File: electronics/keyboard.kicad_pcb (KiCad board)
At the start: 2 copper layers, 243 parts, among them CON1 AVR-ISP-6, J2 CONN_01X02_FEMALE, Q1 Q_NMOS_DGS, Q2 Q_NMOS_DGS, Q3 Q_PMOS_DGS, Q4 Q_NMOS_DGS, Q5 Q_PMOS_DGS, SW1 SW_DPST, SW10 SW_Push, SW11 SW_Push, SW12 SW_Push, SW13 SW_Push, SW14 SW_Push, SW15 SW_Push, SW16 SW_Push, SW17 SW_Push, SW18 SW_Push, SW19 SW_Push, SW2 SW_Push, SW20 SW_Push, SW21 SW_Push, SW22 SW_Push, SW23 SW_Push, SW24 SW_Push, SW25 SW_Push, SW26 SW_Push, SW27 SW_Push, SW28 SW_Push, SW29 SW_Push, SW3 SW_Push, SW30 SW_Push, SW31 SW_Push, SW32 SW_Push, SW33 SW_Push, SW34 SW_Push, SW35 SW_Push, SW36 SW_Push, SW37 SW_Push, SW38 SW_Push, SW39 SW_Push, SW4 SW_Push, SW40 SW_Push, SW41 SW_Push, SW42 SW_Push, SW43 SW_Push, SW44 SW_Push, SW45 SW_Push, SW46 SW_Push, SW47 SW_Push, SW48 SW_Push, SW49 SW_Push, SW5 SW_Push, SW50 SW_Push, SW51 SW_Push, SW52 SW_Push, SW53 SW_Push, SW54 SW_Push, SW55 SW_Push, SW56 SW_Push, SW57 SW_Push, SW58 SW_Push, SW59 SW_Push, SW6 SW_Push, SW60 SW_Push, SW61 SW_Push, SW62 SW_Push, SW63 SW_Push, SW64 SW_Push, SW65 SW_Push, SW66 SW_Push, SW67 SW_Push, SW68 SW_Push, SW69 SW_Push, SW7 SW_Push, SW70 SW_Push, SW71 SW_Push, SW72 SW_Push, SW73 SW_Push, SW74 SW_Push, SW75 SW_Push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

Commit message: Seperated the Buttons from the rest
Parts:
- moved SW43 658.1 mm to (-284.5, 58.4)
- moved SW44 623.4 mm to (-297.2, -77.5)
- moved SW47 623.4 mm to (-268.0, -99.1)
- moved SW42 600.7 mm to (-236.2, -3.81)
- moved SW26 583.9 mm to (-341.6, -88.9)
- moved SW48 578.1 mm to (-238.8, 27.9)
- moved SW12 541.4 mm to (-294.6, 29.2)
- moved SW89 492.8 mm to (-325.1, -41.9)
- moved SW90 492.8 mm to (-276.9, -50.8)
- moved SW91 492.8 mm to (-241.3, -43.2)
- moved SW88 492.8 mm to (-398.8, -41.9)
- moved SW55 421.7 mm to (-407.7, 63.5)
- moved SW56 421.7 mm to (-407.7, 81.3)
- moved SW30 421.7 mm to (-386.1, 8.89)
- moved SW54 421.7 mm to (-408.9, 40.6)
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
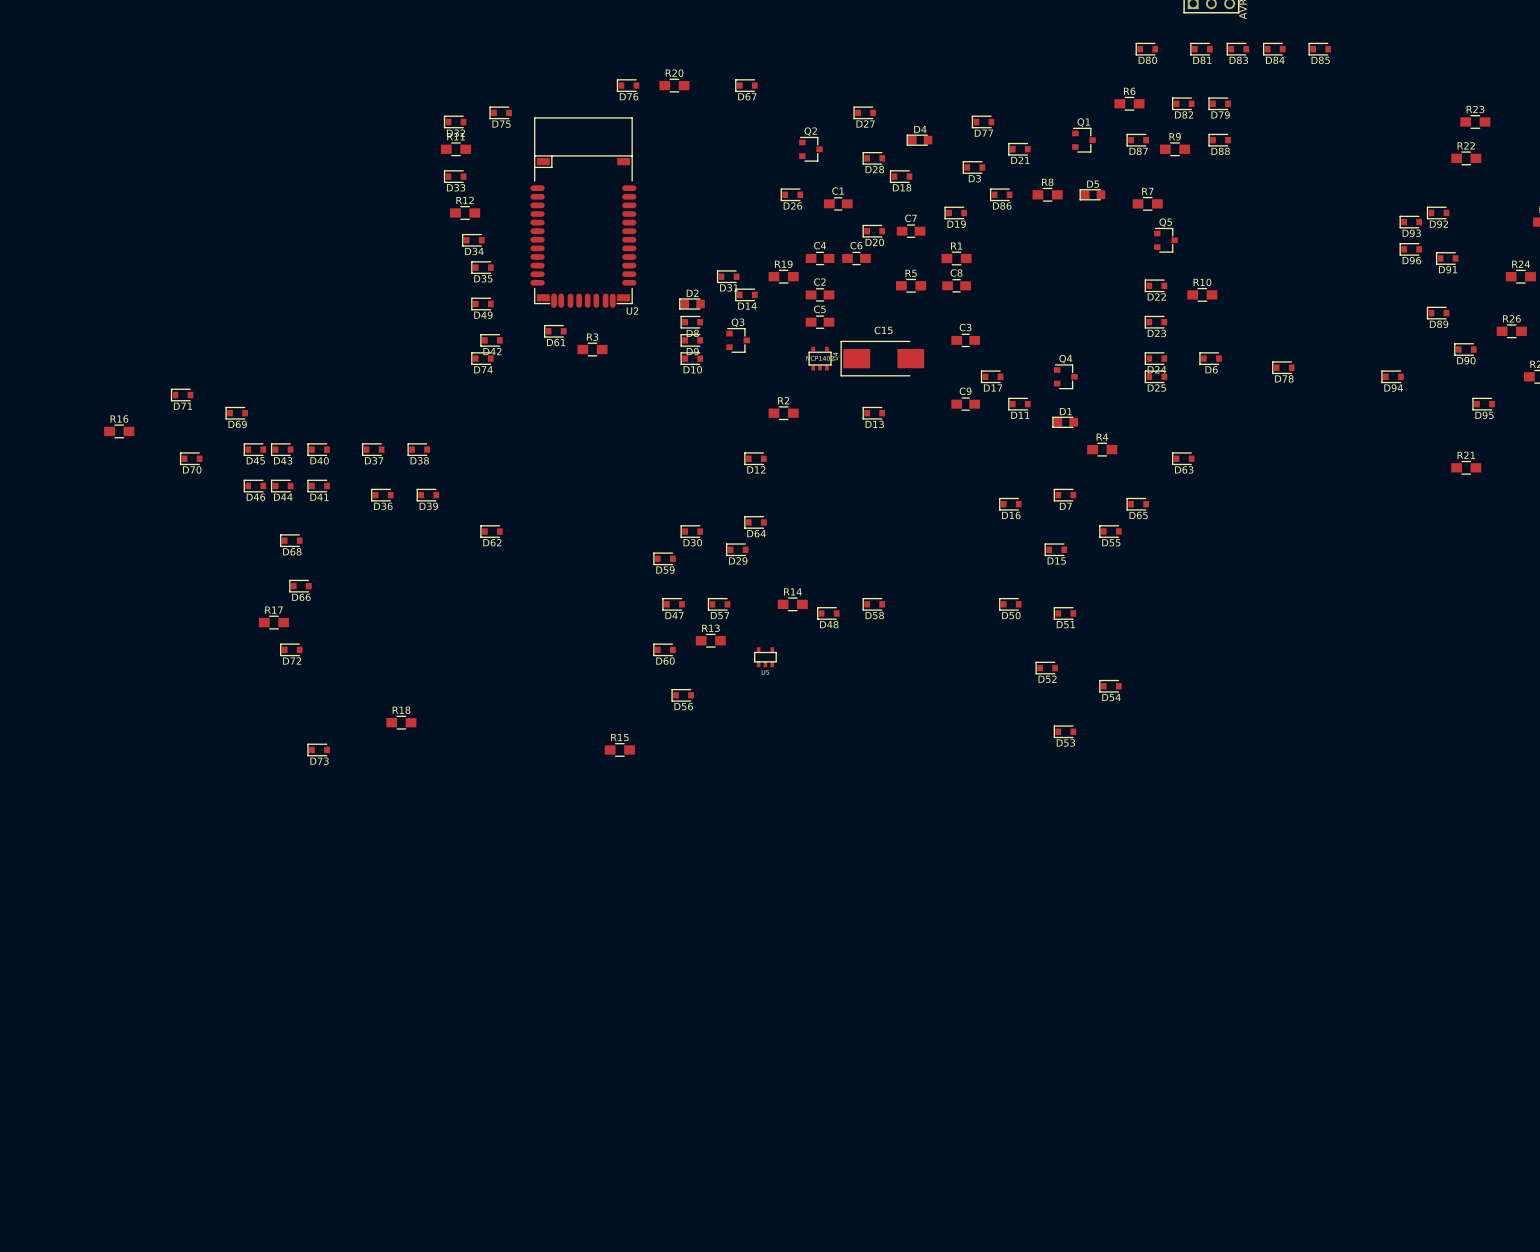
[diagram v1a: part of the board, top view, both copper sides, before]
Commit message: Seperated diodes
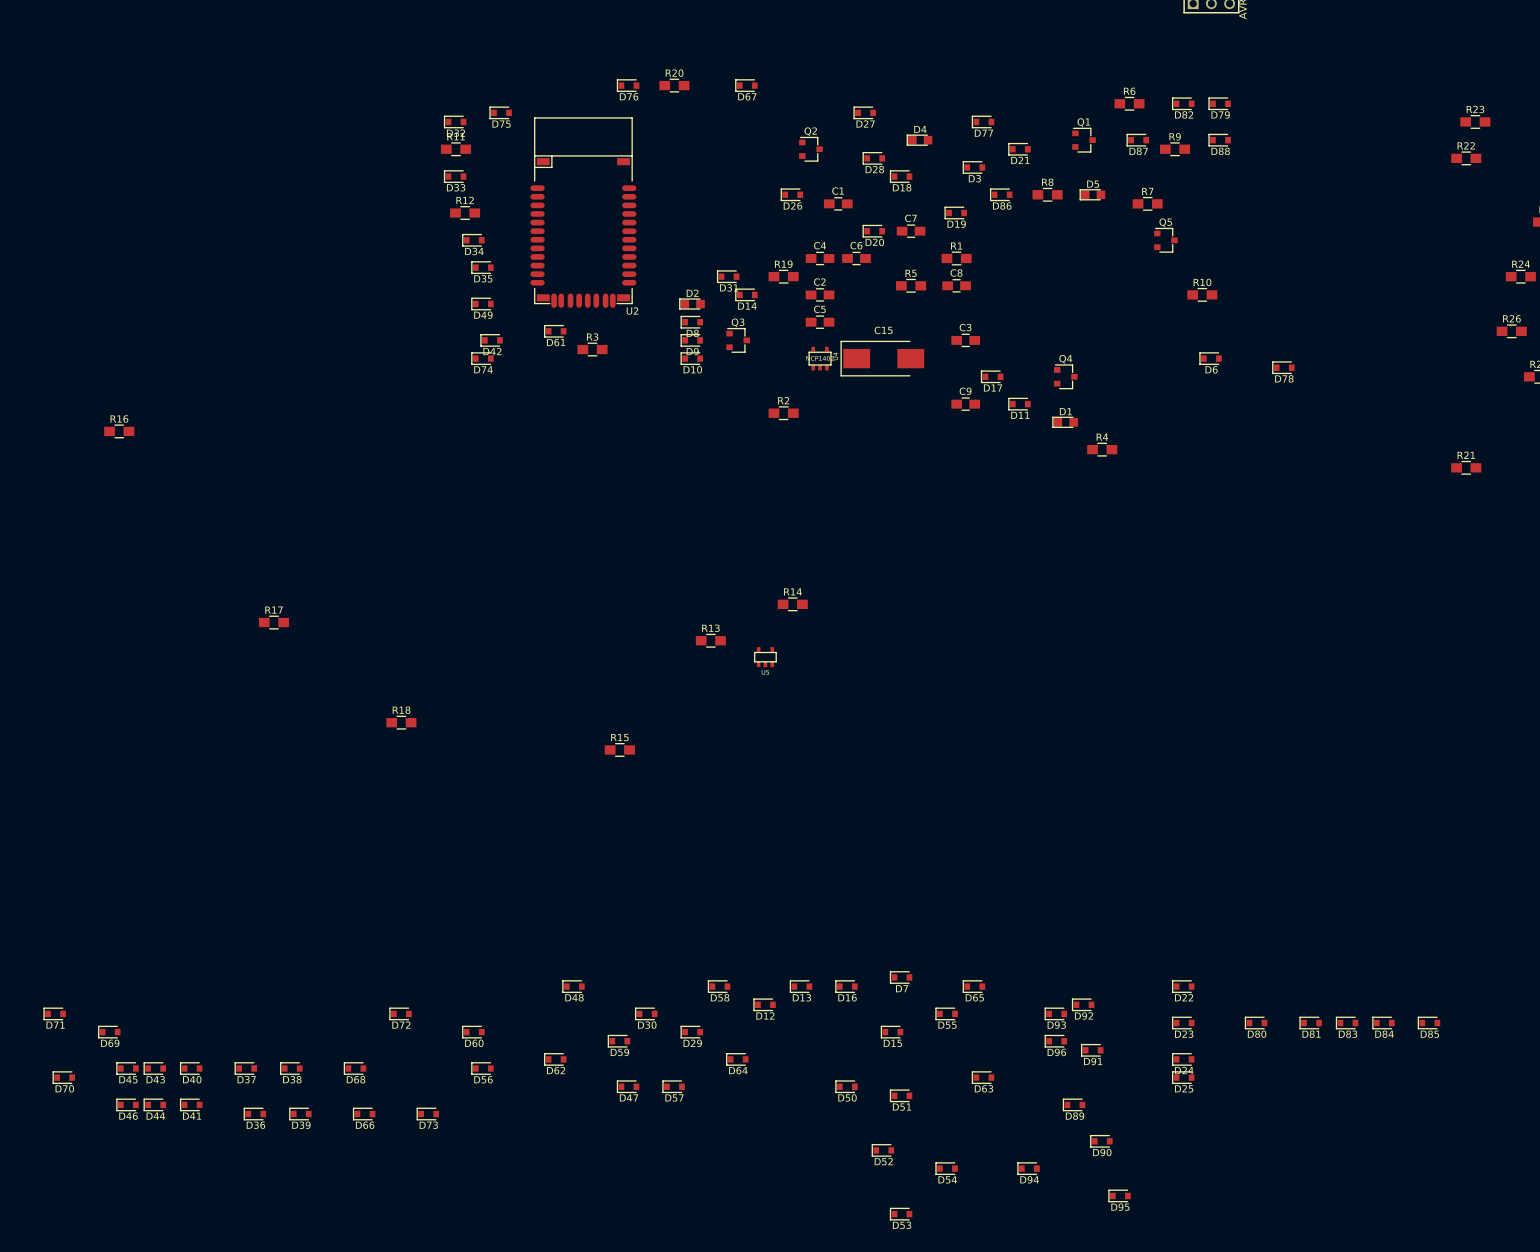
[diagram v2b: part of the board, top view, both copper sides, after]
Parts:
- moved D80 136.7 mm to (198.1, 210.8)
- moved D81 136.7 mm to (205.7, 210.8)
- moved D84 136.7 mm to (215.9, 210.8)
- moved D85 136.7 mm to (222.2, 210.8)
- moved D83 136.7 mm to (210.8, 210.8)
- moved D90 121.6 mm to (176.5, 227.3)
- moved D89 121.6 mm to (172.7, 222.2)
- moved D95 121.6 mm to (179.1, 234.9)
- moved D94 121.6 mm to (166.4, 231.1)
- moved D93 121.1 mm to (170.2, 209.6)
- moved D96 121.1 mm to (170.2, 213.4)
- moved D91 121.1 mm to (175.3, 214.6)
- moved D92 121.1 mm to (174.0, 208.3)
- moved D22 97.9 mm to (188.0, 205.7)
- moved D24 97.9 mm to (188.0, 215.9)
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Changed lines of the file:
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@@
     (links 407)
     (no_connects 407)
-    (area -421.280001 -139.340001 374.575001 230.15)
+    (area -421.280001 -139.340001 374.575001 243.480001)
     (thickness 1.6)
     (drawings 0)
@@
   )
   (module Diodes_SMD:D_0805 (layer F.Cu)
-    (at 171.45 137.16)
+    (at 148.59 204.47)
     (descr "Diode SMD in 0805 package")
     (tags "smd diode")
@@
   )
   (module Diodes_SMD:D_0805 (layer F.Cu)
-    (at 128.27 132.08)
+    (at 129.54 208.28)
     (descr "Diode SMD in 0805 package")
     (tags "smd diode")
@@
   )
   (module Diodes_SMD:D_0805 (layer F.Cu)
-    (at 144.78 125.73)
+    (at 134.62 205.74)
     (descr "Diode SMD in 0805 package")
     (tags "smd diode")
@@
   )
   (module Diodes_SMD:D_0805 (layer F.Cu)
-    (at 170.18 144.78)
+    (at 147.32 212.09)
     (descr "Diode SMD in 0805 package")
     (tags "smd diode")
@@
   )
   (module Diodes_SMD:D_0805 (layer F.Cu)
-    (at 163.83 138.43)
+    (at 140.97 205.74)
     (descr "Diode SMD in 0805 package")
     (tags "smd diode")
@@
   )
   (module Diodes_SMD:D_0805 (layer F.Cu)
-    (at 184.15 107.95)
+    (at 187.96 205.74)
     (descr "Diode SMD in 0805 package")
     (tags "smd diode")
@@
   )
   (module Diodes_SMD:D_0805 (layer F.Cu)
-    (at 184.15 113.03)
+    (at 187.96 210.82)
     (descr "Diode SMD in 0805 package")
     (tags "smd diode")
@@
   )
   (module Diodes_SMD:D_0805 (layer F.Cu)
-    (at 184.15 118.11)
+    (at 187.96 215.9)
     (descr "Diode SMD in 0805 package")
     (tags "smd diode")
@@
   )
   (module Diodes_SMD:D_0805 (layer F.Cu)
-    (at 184.15 120.65)
+    (at 187.96 218.44)
     (descr "Diode SMD in 0805 package")
     (tags "smd diode")
@@
   )
   (module Diodes_SMD:D_0805 (layer F.Cu)
-    (at 125.73 144.78)
+    (at 119.38 212.09)
     (descr "Diode SMD in 0805 package")
     (tags "smd diode")
@@
   )
   (module Diodes_SMD:D_0805 (layer F.Cu)
-    (at 119.38 142.24)
+    (at 113.03 209.55)
     (descr "Diode SMD in 0805 package")
     (tags "smd diode")
@@
   )
   (module Diodes_SMD:D_0805 (layer F.Cu)
-    (at 76.2 137.16)
+    (at 58.42 223.52)
     (descr "Diode SMD in 0805 package")
     (tags "smd diode")
@@
   )
   (module Diodes_SMD:D_0805 (layer F.Cu)
-    (at 74.93 130.81)
+    (at 57.15 217.17)
     (descr "Diode SMD in 0805 package")
     (tags "smd diode")
@@
   )
   (module Diodes_SMD:D_0805 (layer F.Cu)
-    (at 81.28 130.81)
+    (at 63.5 217.17)
     (descr "Diode SMD in 0805 package")
     (tags "smd diode")
@@
   )
   (module Diodes_SMD:D_0805 (layer F.Cu)
-    (at 82.55 137.16)
+    (at 64.77 223.52)
     (descr "Diode SMD in 0805 package")
     (tags "smd diode")
@@
   )
   (module Diodes_SMD:D_0805 (layer F.Cu)
-    (at 67.31 130.81)
+    (at 49.53 217.17)
     (descr "Diode SMD in 0805 package")
     (tags "smd diode")
@@
   )
   (module Diodes_SMD:D_0805 (layer F.Cu)
-    (at 67.31 135.89)
+    (at 49.53 222.25)
     (descr "Diode SMD in 0805 package")
     (tags "smd diode")
@@
   )
   (module Diodes_SMD:D_0805 (layer F.Cu)
-    (at 62.23 130.81)
+    (at 44.45 217.17)
     (descr "Diode SMD in 0805 package")
     (tags "smd diode")
@@
   )
   (module Diodes_SMD:D_0805 (layer F.Cu)
-    (at 62.23 135.89)
+    (at 44.45 222.25)
     (descr "Diode SMD in 0805 package")
     (tags "smd diode")
@@
   )
   (module Diodes_SMD:D_0805 (layer F.Cu)
-    (at 58.42 130.81)
+    (at 40.64 217.17)
     (descr "Diode SMD in 0805 package")
     (tags "smd diode")
@@
   )
   (module Diodes_SMD:D_0805 (layer F.Cu)
-    (at 58.42 135.89)
+    (at 40.64 222.25)
     (descr "Diode SMD in 0805 package")
     (tags "smd diode")
@@
   )
   (module Diodes_SMD:D_0805 (layer F.Cu)
-    (at 116.84 152.4)
+    (at 110.49 219.71)
     (descr "Diode SMD in 0805 package")
     (tags "smd diode")
@@
   )
   (module Diodes_SMD:D_0805 (layer F.Cu)
-    (at 138.43 153.67)
+    (at 102.87 205.74)
     (descr "Diode SMD in 0805 package")
     (tags "smd diode")
@@
   )
   (module Diodes_SMD:D_0805 (layer F.Cu)
-    (at 163.83 152.4)
+    (at 140.97 219.71)
     (descr "Diode SMD in 0805 package")
     (tags "smd diode")
@@
   )
   (module Diodes_SMD:D_0805 (layer F.Cu)
-    (at 171.45 153.67)
+    (at 148.59 220.98)
     (descr "Diode SMD in 0805 package")
     (tags "smd diode")
@@
   )
   (module Diodes_SMD:D_0805 (layer F.Cu)
-    (at 168.91 161.29)
+    (at 146.05 228.6)
     (descr "Diode SMD in 0805 package")
     (tags "smd diode")
@@
   )
   (module Diodes_SMD:D_0805 (layer F.Cu)
-    (at 171.45 170.18)
+    (at 148.59 237.49)
     (descr "Diode SMD in 0805 package")
     (tags "smd diode")
@@
   )
   (module Diodes_SMD:D_0805 (layer F.Cu)
-    (at 177.8 163.83)
+    (at 154.94 231.14)
     (descr "Diode SMD in 0805 package")
     (tags "smd diode")
@@
   )
   (module Diodes_SMD:D_0805 (layer F.Cu)
-    (at 177.8 142.24)
+    (at 154.94 209.55)
     (descr "Diode SMD in 0805 package")
     (tags "smd diode")
@@
   )
   (module Diodes_SMD:D_0805 (layer F.Cu)
-    (at 118.11 165.1)
+    (at 90.17 217.17)
     (descr "Diode SMD in 0805 package")
     (tags "smd diode")
@@
   )
   (module Diodes_SMD:D_0805 (layer F.Cu)
-    (at 123.19 152.4)
+    (at 116.84 219.71)
     (descr "Diode SMD in 0805 package")
     (tags "smd diode")
@@
   )
   (module Diodes_SMD:D_0805 (layer F.Cu)
-    (at 144.78 152.4)
+    (at 123.19 205.74)
     (descr "Diode SMD in 0805 package")
     (tags "smd diode")
@@
   )
   (module Diodes_SMD:D_0805 (layer F.Cu)
-    (at 115.57 146.05)
+    (at 109.22 213.36)
     (descr "Diode SMD in 0805 package")
     (tags "smd diode")
@@
   )
   (module Diodes_SMD:D_0805 (layer F.Cu)
-    (at 115.57 158.75)
+    (at 88.9 212.09)
     (descr "Diode SMD in 0805 package")
     (tags "smd diode")
@@
   )
   (module Diodes_SMD:D_0805 (layer F.Cu)
-    (at 91.44 142.24)
+    (at 100.33 215.9)
     (descr "Diode SMD in 0805 package")
     (tags "smd diode")
@@
   )
   (module Diodes_SMD:D_0805 (layer F.Cu)
-    (at 187.96 132.08)
+    (at 160.02 218.44)
     (descr "Diode SMD in 0805 package")
     (tags "smd diode")
@@
   )
   (module Diodes_SMD:D_0805 (layer F.Cu)
-    (at 128.27 140.97)
+    (at 125.73 215.9)
     (descr "Diode SMD in 0805 package")
     (tags "smd diode")
@@
   )
   (module Diodes_SMD:D_0805 (layer F.Cu)
-    (at 181.61 138.43)
+    (at 158.75 205.74)
     (descr "Diode SMD in 0805 package")
     (tags "smd diode")
@@
   )
   (module Diodes_SMD:D_0805 (layer F.Cu)
-    (at 64.77 149.86)
+    (at 73.66 223.52)
     (descr "Diode SMD in 0805 package")
     (tags "smd diode")
@@
   )
   (module Diodes_SMD:D_0805 (layer F.Cu)
-    (at 63.5 143.51)
+    (at 72.39 217.17)
     (descr "Diode SMD in 0805 package")
     (tags "smd diode")
@@
   )
   (module Diodes_SMD:D_0805 (layer F.Cu)
-    (at 55.88 125.73)
+    (at 38.1 212.09)
     (descr "Diode SMD in 0805 package")
     (tags "smd diode")
@@
   )
   (module Diodes_SMD:D_0805 (layer F.Cu)
-    (at 49.53 132.08)
+    (at 31.75 218.44)
     (descr "Diode SMD in 0805 package")
     (tags "smd diode")
@@
   )
   (module Diodes_SMD:D_0805 (layer F.Cu)
-    (at 48.26 123.19)
+    (at 30.48 209.55)
     (descr "Diode SMD in 0805 package")
     (tags "smd diode")
@@
   )
   (module Diodes_SMD:D_0805 (layer F.Cu)
-    (at 63.5 158.75)
+    (at 78.74 209.55)
     (descr "Diode SMD in 0805 package")
     (tags "smd diode")
@@
   )
   (module Diodes_SMD:D_0805 (layer F.Cu)
-    (at 67.31 172.72)
+    (at 82.55 223.52)
     (descr "Diode SMD in 0805 package")
     (tags "smd diode")
@@
   )
   (module Diodes_SMD:D_0805 (layer F.Cu)
-    (at 182.88 74.93)
+    (at 198.12 210.82)
     (descr "Diode SMD in 0805 package")
     (tags "smd diode")
@@
   )
   (module Diodes_SMD:D_0805 (layer F.Cu)
-    (at 190.5 74.93)
+    (at 205.74 210.82)
     (descr "Diode SMD in 0805 package")
     (tags "smd diode")
@@
   )
   (module Diodes_SMD:D_0805 (layer F.Cu)
-    (at 195.58 74.93)
+    (at 210.82 210.82)
     (descr "Diode SMD in 0805 package")
     (tags "smd diode")
@@
   )
   (module Diodes_SMD:D_0805 (layer F.Cu)
-    (at 200.66 74.93)
+    (at 215.9 210.82)
     (descr "Diode SMD in 0805 package")
     (tags "smd diode")
@@
   )
   (module Diodes_SMD:D_0805 (layer F.Cu)
-    (at 207.01 74.93)
+    (at 222.25 210.82)
     (descr "Diode SMD in 0805 package")
     (tags "smd diode")
@@
   )
   (module Diodes_SMD:D_0805 (layer F.Cu)
-    (at 223.52 111.76)
+    (at 172.72 222.25)
     (descr "Diode SMD in 0805 package")
     (tags "smd diode")
@@
   )
   (module Diodes_SMD:D_0805 (layer F.Cu)
-    (at 227.33 116.84)
+    (at 176.53 227.33)
     (descr "Diode SMD in 0805 package")
     (tags "smd diode")
@@
   )
   (module Diodes_SMD:D_0805 (layer F.Cu)
-    (at 224.79 104.14)
+    (at 175.26 214.63)
     (descr "Diode SMD in 0805 package")
     (tags "smd diode")
@@
   )
   (module Diodes_SMD:D_0805 (layer F.Cu)
-    (at 223.52 97.79)
+    (at 173.99 208.28)
     (descr "Diode SMD in 0805 package")
     (tags "smd diode")
@@
   )
   (module Diodes_SMD:D_0805 (layer F.Cu)
-    (at 219.71 99.06)
+    (at 170.18 209.55)
     (descr "Diode SMD in 0805 package")
     (tags "smd diode")
@@
   )
   (module Diodes_SMD:D_0805 (layer F.Cu)
-    (at 217.17 120.65)
+    (at 166.37 231.14)
     (descr "Diode SMD in 0805 package")
     (tags "smd diode")
@@
   )
   (module Diodes_SMD:D_0805 (layer F.Cu)
-    (at 229.87 124.46)
+    (at 179.07 234.95)
     (descr "Diode SMD in 0805 package")
     (tags "smd diode")
@@
   )
   (module Diodes_SMD:D_0805 (layer F.Cu)
-    (at 219.71 102.87)
+    (at 170.18 213.36)
     (descr "Diode SMD in 0805 package")
     (tags "smd diode")

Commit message: seperated elements for the controller
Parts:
- moved R3 215.3 mm to (308.6, 188.0)
- moved R2 213.2 mm to (339.1, 176.5)
- moved C6 207.3 mm to (327.7, 196.8)
- moved C1 203.0 mm to (316.2, 196.8)
- moved C7 200.5 mm to (337.8, 170.2)
- moved CON1 195.8 mm to (334.0, 201.9)
- moved C2 190.8 mm to (317.5, 171.4)
- moved C4 189.2 mm to (317.5, 161.3)
- moved D67 187.4 mm to (232.4, 234.9)
- moved C5 185.4 mm to (317.5, 156.2)
- moved D75 177.3 mm to (201.9, 223.5)
- moved D32 176.3 mm to (195.6, 223.5)
- moved D26 175.8 mm to (246.4, 229.9)
- moved D18 168.4 mm to (238.8, 234.9)
- moved D27 168.4 mm to (233.7, 226.1)
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
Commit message: Clustured Suplly Circuitry
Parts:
- moved U4 214.1 mm to (349.2, 17.8)
- moved Q4 195.0 mm to (375.9, 67.3)
- moved R19 181.3 mm to (326.4, 69.8), turned to 180 degrees
- moved D4 180.5 mm to (327.7, 40.6)
- moved R27 179.7 mm to (396.2, 66.0)
- moved Q5 178.4 mm to (375.9, 61.0)
- moved R25 175.8 mm to (388.6, 69.8)
- moved R26 175.8 mm to (384.8, 63.5)
- moved D5 175.2 mm to (327.7, 44.5)
- moved R21 171.5 mm to (334.0, 44.5)
- moved D6 171.4 mm to (345.4, 14.0), turned to 180 degrees
- moved R23 158.3 mm to (384.8, 59.7)
- moved D3 153.9 mm to (326.4, 61.0)
- moved U3 145.5 mm to (395.0, 20.3)
- moved Q3 131.4 mm to (334.0, 66.0)
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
